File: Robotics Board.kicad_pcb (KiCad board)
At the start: 2 copper layers, 102 parts, among them CON1 DC_IN, J1 USB, K1 CONN_3, K2 CONN_3, P1 CONN_3, P10 CONN_6, P11 CONN_8, P12 CONN_12, P13 CONN_6, P14 CONN_12, P15 CONN_5, P16 CONN_12, P17 CONN_12, P18 CONN_12, P19 CONN_12, P2 CONN_3, P20 CONN_12, P21 CONN_12, P22 CONN_12, P23 CONN_1, P24 CONN_12, P3 CONN_12, P4 CONN_12, P5 CONN_12, P6 CONN_12, P7 CONN_12, P8 CONN_8, P9 CONN_8, U1 7805, U2 L293, U3 PIC18F4550, U4 MCP2200, U5 3.3VREG, X1 4MHz, X2 12MHz

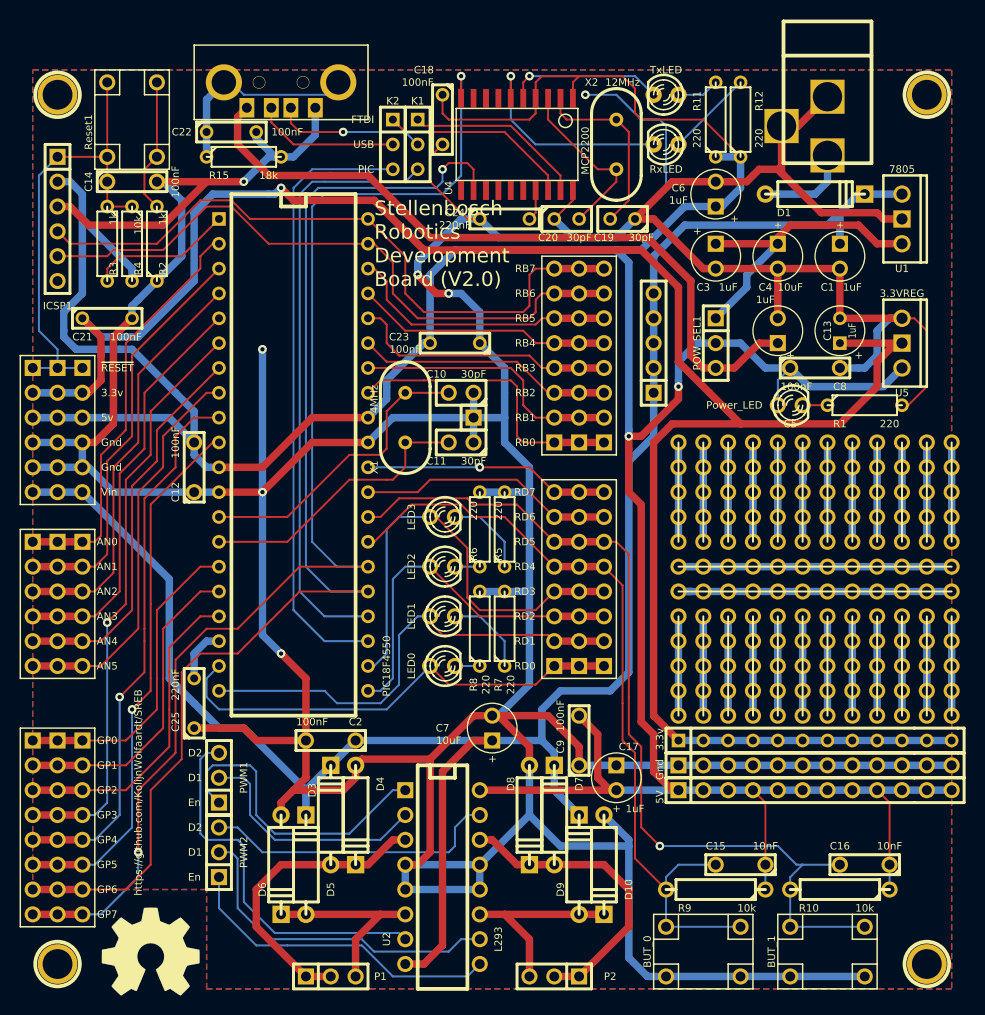
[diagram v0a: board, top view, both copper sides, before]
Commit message: Changed some silkscreen, added ground pane keepout under crystal and MCP2200
Signed-off-by: Kolijn Wolfaardt <kolijn.wolfaardt@gmail.com>
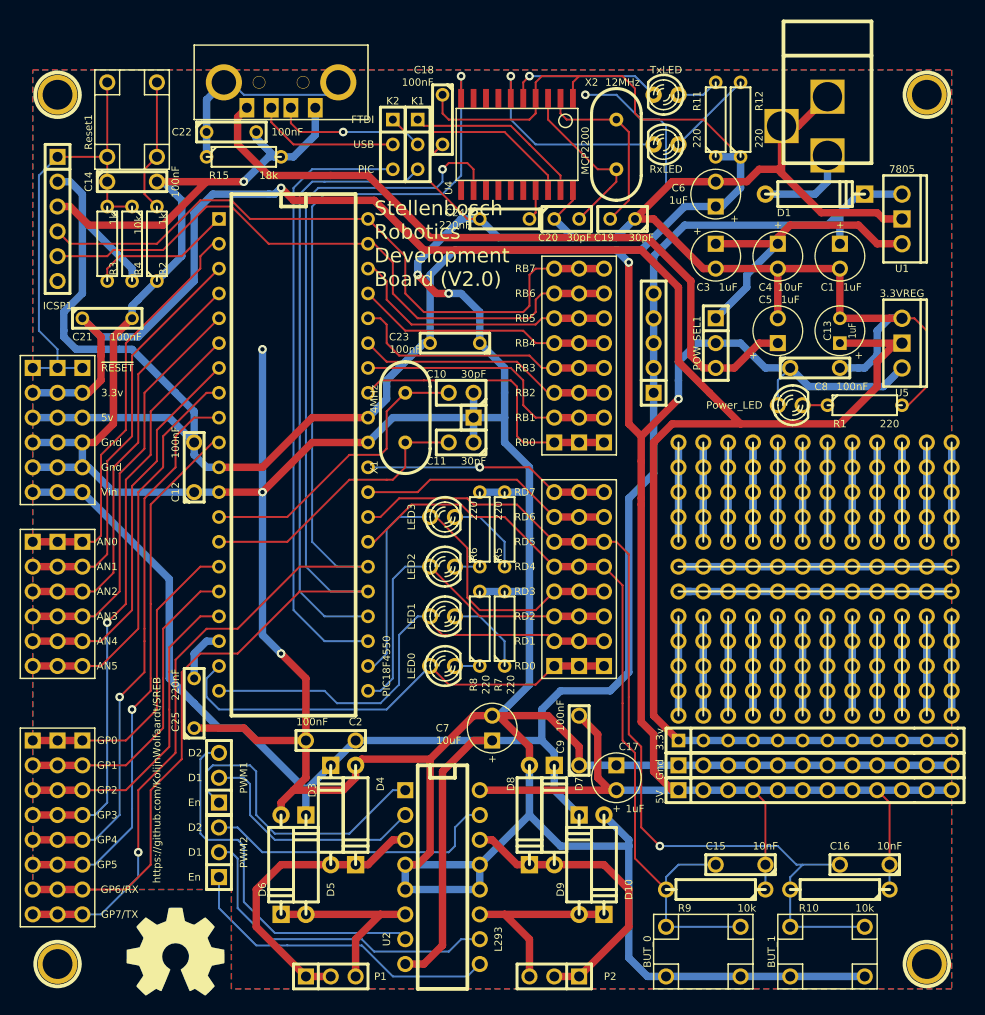
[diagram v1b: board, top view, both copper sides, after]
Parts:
- moved OSHWLogoBack1 2.54 mm to (78.1, 142.2)
- moved OSHWLogoFront1 2.54 mm to (78.1, 142.2)
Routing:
- net V_5v: track 366.9 -> 365.6 mm
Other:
- board text added: "GP6/RX"
- board text added: "GP7/TX"
- board text removed: "GP6"
- board text removed: "GP7"

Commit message: Changed Via size, at PCB fab's request.
Signed-off-by: Kolijn Wolfaardt <kolijn.wolfaardt@gmail.com>
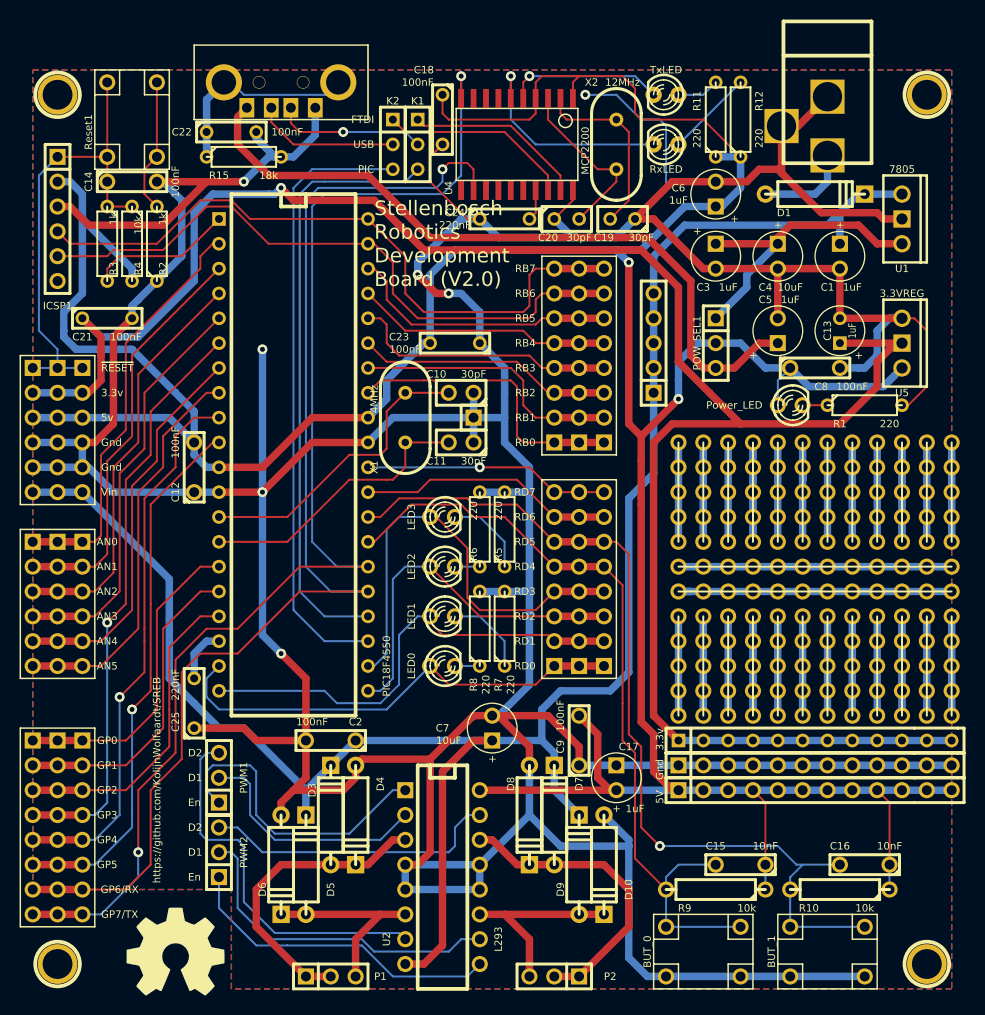
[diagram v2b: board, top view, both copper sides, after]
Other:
- net class Default: via_dia 0.889 -> 1.016
- rule via_min_size: 0.889 -> 1.016
